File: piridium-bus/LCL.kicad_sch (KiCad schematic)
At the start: 12 parts

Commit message: add R5460 and small bom edits
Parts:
- R?: value 500K -> 510K
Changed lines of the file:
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@@
   (symbol (lib_id "power:GND") (at 148.59 106.68 0) (unit 1)
     (in_bom yes) (on_board yes)
-    (property "Reference" "#PWR?" (id 0) (at 148.59 113.03 0)
+    (property "Reference" "#PWR0105" (id 0) (at 148.59 113.03 0)
       (effects (font (size 1.27 1.27)) hide)
     )
@@
   (symbol (lib_id "power:+3.3VA") (at 125.73 78.74 0) (unit 1)
     (in_bom yes) (on_board yes) (fields_autoplaced)
-    (property "Reference" "#PWR?" (id 0) (at 125.73 82.55 0)
+    (property "Reference" "#PWR0104" (id 0) (at 125.73 82.55 0)
       (effects (font (size 1.27 1.27)) hide)
     )
@@
   (symbol (lib_id "power:GND") (at 95.25 87.63 0) (unit 1)
     (in_bom yes) (on_board yes)
-    (property "Reference" "#PWR?" (id 0) (at 95.25 93.98 0)
+    (property "Reference" "#PWR0108" (id 0) (at 95.25 93.98 0)
       (effects (font (size 1.27 1.27)) hide)
     )
@@
   (symbol (lib_id "power:+3.3VA") (at 95.25 80.01 0) (unit 1)
     (in_bom yes) (on_board yes)
-    (property "Reference" "#PWR?" (id 0) (at 95.25 83.82 0)
+    (property "Reference" "#PWR0107" (id 0) (at 95.25 83.82 0)
       (effects (font (size 1.27 1.27)) hide)
     )
@@
     (in_bom yes) (on_board yes)
     (property "Reference" "R?" (id 0) (at 120.65 96.52 90))
-    (property "Value" "500K" (id 1) (at 120.65 99.06 90))
+    (property "Value" "510K" (id 1) (at 120.65 99.06 90))
     (property "Footprint" "Resistor_SMD:R_0805_2012Metric" (id 2) (at 120.65 100.838 90)
       (effects (font (size 1.27 1.27)) hide)
@@
   (symbol (lib_id "power:+3.3VA") (at 106.68 93.98 0) (unit 1)
     (in_bom yes) (on_board yes)
-    (property "Reference" "#PWR?" (id 0) (at 106.68 97.79 0)
-      (effects (font (size 1.27 1.27)) hide)
-    )
+    (property "Reference" "#PWR0106" (id 0) (at 106.68 97.79 0)
+      (effects (font (size 1.27 1.27)) hide)
+    )

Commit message: battery sch finish
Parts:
- gave numbers to parts that had none: 12
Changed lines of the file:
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@@
   (symbol (lib_id "Transistor_FET:IRF7404") (at 115.57 73.66 270) (mirror x) (unit 1)
     (in_bom yes) (on_board yes)
-    (property "Reference" "Q?" (id 0) (at 115.57 64.9732 90))
+    (property "Reference" "Q9" (id 0) (at 115.57 64.9732 90))
     (property "Value" "DMP3015LSSQ" (id 1) (at 115.57 67.2846 90))
     (property "Footprint" "Package_SO:SOIC-8_3.9x4.9mm_P1.27mm" (id 2) (at 113.665 68.58 0)
@@
   (symbol (lib_id "power:GND") (at 148.59 106.68 0) (unit 1)
     (in_bom yes) (on_board yes)
-    (property "Reference" "#PWR0105" (id 0) (at 148.59 113.03 0)
+    (property "Reference" "#PWR068" (id 0) (at 148.59 113.03 0)
       (effects (font (size 1.27 1.27)) hide)
     )
@@
   (symbol (lib_id "power:+3.3VA") (at 125.73 78.74 0) (unit 1)
     (in_bom yes) (on_board yes) (fields_autoplaced)
-    (property "Reference" "#PWR0104" (id 0) (at 125.73 82.55 0)
+    (property "Reference" "#PWR067" (id 0) (at 125.73 82.55 0)
       (effects (font (size 1.27 1.27)) hide)
     )
@@
   (symbol (lib_id "Device:R") (at 110.49 74.93 0) (mirror y) (unit 1)
     (in_bom yes) (on_board yes)
-    (property "Reference" "R?" (id 0) (at 109.22 74.93 0)
+    (property "Reference" "R43" (id 0) (at 109.22 74.93 0)
       (effects (font (size 1.27 1.27)) (justify left))
     )
@@
   (symbol (lib_id "74xGxx:SN74LVC1G14DBV") (at 106.68 99.06 0) (unit 1)
     (in_bom yes) (on_board yes)
-    (property "Reference" "U?" (id 0) (at 102.87 102.87 0)
+    (property "Reference" "U13" (id 0) (at 102.87 102.87 0)
       (effects (font (size 1.27 1.27)) (justify right))
     )
@@
   (symbol (lib_id "Transistor_FET:2N7002") (at 118.11 83.82 0) (mirror y) (unit 1)
     (in_bom yes) (on_board yes)
-    (property "Reference" "Q?" (id 0) (at 112.903 82.6516 0)
+    (property "Reference" "Q10" (id 0) (at 112.903 82.6516 0)
       (effects (font (size 1.27 1.27)) (justify left))
     )
@@
   (symbol (lib_id "Device:R") (at 148.59 71.12 270) (unit 1)
     (in_bom yes) (on_board yes)
-    (property "Reference" "R?" (id 0) (at 148.59 68.58 90))
+    (property "Reference" "R47" (id 0) (at 148.59 68.58 90))
     (property "Value" "10m" (id 1) (at 148.59 71.12 90))
     (property "Footprint" "Resistor_SMD:R_1206_3216Metric" (id 2) (at 148.59 69.342 90)
@@
   (symbol (lib_id "Device:C") (at 95.25 83.82 0) (unit 1)
     (in_bom yes) (on_board yes)
-    (property "Reference" "C?" (id 0) (at 98.171 82.6516 0)
+    (property "Reference" "C32" (id 0) (at 98.171 82.6516 0)
       (effects (font (size 1.27 1.27)) (justify left))
     )
@@
   (symbol (lib_id "Device:R") (at 132.08 88.9 0) (unit 1)
     (in_bom yes) (on_board yes)
-    (property "Reference" "R?" (id 0) (at 133.35 88.9 0)
+    (property "Reference" "R46" (id 0) (at 133.35 88.9 0)
       (effects (font (size 1.27 1.27)) (justify left))
     )
@@
   (symbol (lib_id "Device:C") (at 124.46 102.87 0) (mirror y) (unit 1)
     (in_bom yes) (on_board yes)
-    (property "Reference" "C?" (id 0) (at 121.92 101.6 0)
+    (property "Reference" "C33" (id 0) (at 121.92 101.6 0)
       (effects (font (size 1.27 1.27)) (justify left))
     )
@@
   (symbol (lib_id "power:GND") (at 95.25 87.63 0) (unit 1)
     (in_bom yes) (on_board yes)
-    (property "Reference" "#PWR0108" (id 0) (at 95.25 93.98 0)
+    (property "Reference" "#PWR065" (id 0) (at 95.25 93.98 0)
       (effects (font (size 1.27 1.27)) hide)
     )
@@
   (symbol (lib_id "Transistor_FET:2N7002") (at 129.54 99.06 0) (unit 1)
     (in_bom yes) (on_board yes)
-    (property "Reference" "Q?" (id 0) (at 134.747 97.8916 0)
+    (property "Reference" "Q11" (id 0) (at 134.747 97.8916 0)
       (effects (font (size 1.27 1.27)) (justify left))
     )
@@
   (symbol (lib_id "Device:R") (at 125.73 82.55 0) (unit 1)
     (in_bom yes) (on_board yes)
-    (property "Reference" "R?" (id 0) (at 127 82.55 0)
+    (property "Reference" "R45" (id 0) (at 127 82.55 0)
       (effects (font (size 1.27 1.27)) (justify left))
     )
@@
   (symbol (lib_id "power:+3.3VA") (at 95.25 80.01 0) (unit 1)
     (in_bom yes) (on_board yes)
-    (property "Reference" "#PWR0107" (id 0) (at 95.25 83.82 0)
+    (property "Reference" "#PWR064" (id 0) (at 95.25 83.82 0)
       (effects (font (size 1.27 1.27)) hide)
     )
@@
   (symbol (lib_id "Device:R") (at 120.65 99.06 90) (unit 1)
     (in_bom yes) (on_board yes)
-    (property "Reference" "R?" (id 0) (at 120.65 96.52 90))
+    (property "Reference" "R44" (id 0) (at 120.65 96.52 90))
     (property "Value" "510K" (id 1) (at 120.65 99.06 90))
     (property "Footprint" "Resistor_SMD:R_0805_2012Metric" (id 2) (at 120.65 100.838 90)
@@
   (symbol (lib_id "piridium-bus:MAX4373F") (at 148.59 76.2 0) (unit 1)
     (in_bom yes) (on_board yes)
-    (property "Reference" "U?" (id 0) (at 153.67 72.39 0)
+    (property "Reference" "U14" (id 0) (at 153.67 72.39 0)
       (effects (font (size 1.27 1.27)) (justify left))
     )
@@
   (symbol (lib_id "power:+3.3VA") (at 106.68 93.98 0) (unit 1)
     (in_bom yes) (on_board yes)
-    (property "Reference" "#PWR0106" (id 0) (at 106.68 97.79 0)
-      (effects (font (size 1.27 1.27)) hide)
-    )
+    (property "Reference" "#PWR066" (id 0) (at 106.68 97.79 0)
+      (effects (font (size 1.27 1.27)) hide)
+    )

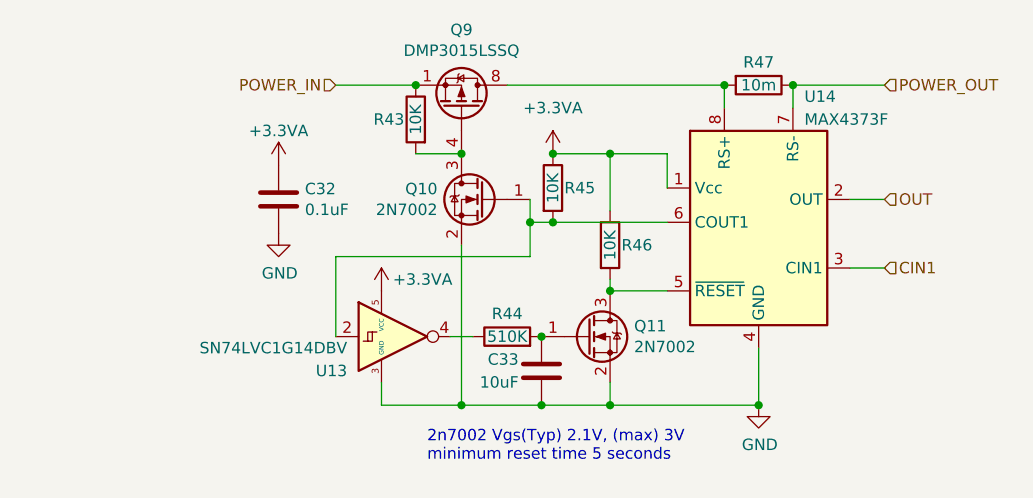
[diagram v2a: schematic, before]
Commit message: correct max4373 implementation, #5 and #4
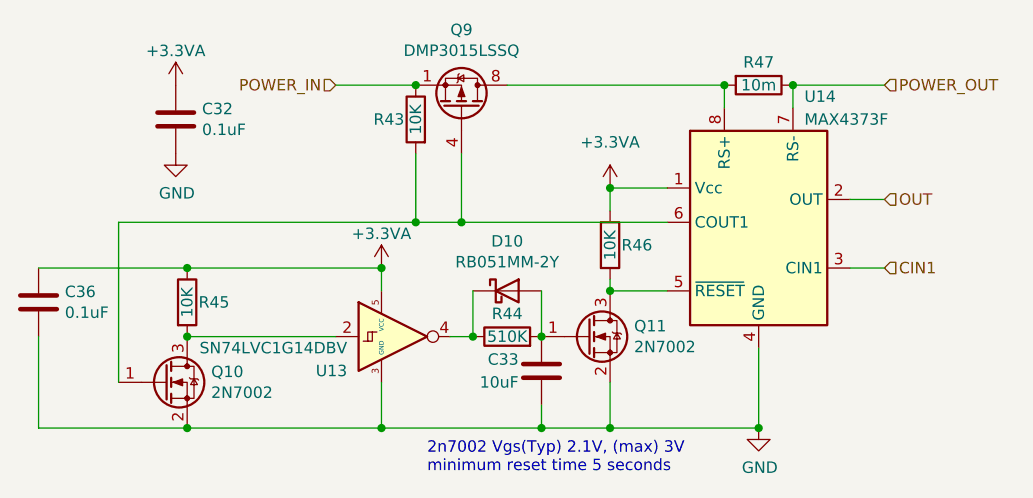
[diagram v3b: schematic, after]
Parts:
- added C36: 0.1uF, Capacitor_SMD:C_0805_2012Metric, symbol Device:C
- added D10: RB051MM-2Y, Diode_SMD:D_SOD-123F, symbol Device:D_Schottky
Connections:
- net +3.3VA: now also C36.1
- net GND: now also C36.2
- net at Q9.4 (G), R43.2: now also Q10.1 (G), U14.6 (COUT1); no longer Q10.3 (D)
- net at R45.2, U13.2: now also Q10.3 (D); no longer Q10.1 (G), U14.6 (COUT1)
- net at R44.1, U13.4: now also D10.1 (K)
- net at C33.1, Q11.1 (G), R44.2: now also D10.2 (A)
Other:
- moved on the sheet: C32

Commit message: mcp3208 constant reference
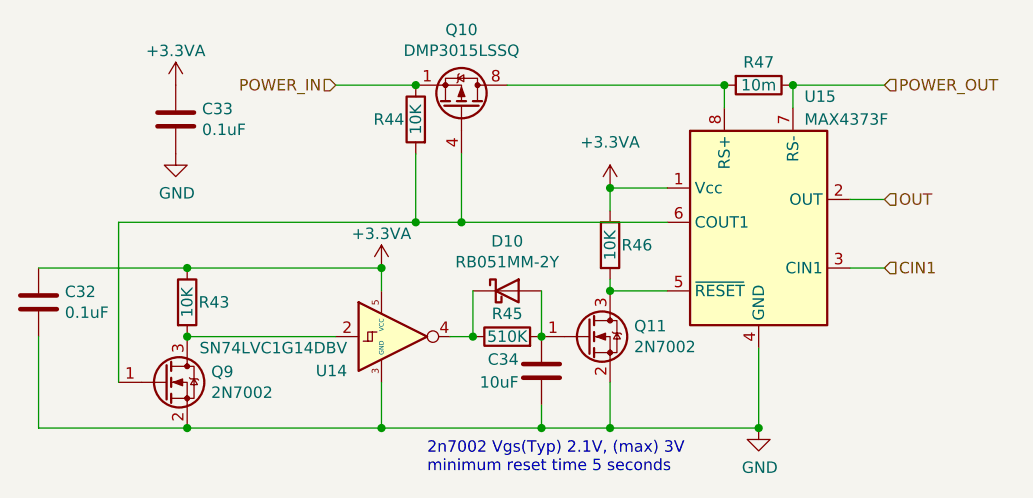
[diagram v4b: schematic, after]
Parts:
- renumbered C36 to C32, C32 to C33, C33 to C34, Q9 to Q10, Q10 to Q9, R45 to R43, R43 to R44, R44 to R45, U13 to U14, U14 to U15
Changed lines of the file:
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@@
   (symbol (lib_id "Transistor_FET:IRF7404") (at 115.57 73.66 270) (mirror x) (unit 1)
     (in_bom yes) (on_board yes)
-    (property "Reference" "Q9" (id 0) (at 115.57 64.9732 90))
+    (property "Reference" "Q10" (id 0) (at 115.57 64.9732 90))
     (property "Value" "DMP3015LSSQ" (id 1) (at 115.57 67.2846 90))
     (property "Footprint" "Package_SO:SOIC-8_3.9x4.9mm_P1.27mm" (id 2) (at 113.665 68.58 0)
@@
   (symbol (lib_id "power:GND") (at 148.59 109.22 0) (unit 1)
     (in_bom yes) (on_board yes)
-    (property "Reference" "#PWR068" (id 0) (at 148.59 115.57 0)
+    (property "Reference" "#PWR070" (id 0) (at 148.59 115.57 0)
       (effects (font (size 1.27 1.27)) hide)
     )
@@
   (symbol (lib_id "power:+3.3VA") (at 132.08 82.55 0) (unit 1)
     (in_bom yes) (on_board yes) (fields_autoplaced)
-    (property "Reference" "#PWR067" (id 0) (at 132.08 86.36 0)
+    (property "Reference" "#PWR069" (id 0) (at 132.08 86.36 0)
       (effects (font (size 1.27 1.27)) hide)
     )
@@
   (symbol (lib_id "Device:R") (at 85.09 95.25 0) (unit 1)
     (in_bom yes) (on_board yes)
-    (property "Reference" "R45" (id 0) (at 86.36 95.25 0)
+    (property "Reference" "R43" (id 0) (at 86.36 95.25 0)
       (effects (font (size 1.27 1.27)) (justify left))
     )
@@
   (symbol (lib_id "Device:R") (at 110.49 74.93 0) (mirror y) (unit 1)
     (in_bom yes) (on_board yes)
-    (property "Reference" "R43" (id 0) (at 109.22 74.93 0)
+    (property "Reference" "R44" (id 0) (at 109.22 74.93 0)
       (effects (font (size 1.27 1.27)) (justify left))
     )
@@
   (symbol (lib_id "74xGxx:SN74LVC1G14DBV") (at 106.68 99.06 0) (unit 1)
     (in_bom yes) (on_board yes)
-    (property "Reference" "U13" (id 0) (at 102.87 102.87 0)
+    (property "Reference" "U14" (id 0) (at 102.87 102.87 0)
       (effects (font (size 1.27 1.27)) (justify right))
     )
@@
   (symbol (lib_id "Device:C") (at 83.82 74.93 0) (unit 1)
     (in_bom yes) (on_board yes)
-    (property "Reference" "C32" (id 0) (at 86.741 73.7616 0)
+    (property "Reference" "C33" (id 0) (at 86.741 73.7616 0)
       (effects (font (size 1.27 1.27)) (justify left))
     )
@@
   (symbol (lib_id "Transistor_FET:2N7002") (at 82.55 104.14 0) (unit 1)
     (in_bom yes) (on_board yes)
-    (property "Reference" "Q10" (id 0) (at 87.757 102.9716 0)
+    (property "Reference" "Q9" (id 0) (at 87.757 102.9716 0)
       (effects (font (size 1.27 1.27)) (justify left))
     )
@@
   (symbol (lib_id "Device:C") (at 124.46 102.87 0) (mirror y) (unit 1)
     (in_bom yes) (on_board yes)
-    (property "Reference" "C33" (id 0) (at 121.92 101.6 0)
+    (property "Reference" "C34" (id 0) (at 121.92 101.6 0)
       (effects (font (size 1.27 1.27)) (justify left))
     )
@@
   (symbol (lib_id "power:GND") (at 83.82 78.74 0) (unit 1)
     (in_bom yes) (on_board yes)
-    (property "Reference" "#PWR065" (id 0) (at 83.82 85.09 0)
+    (property "Reference" "#PWR067" (id 0) (at 83.82 85.09 0)
       (effects (font (size 1.27 1.27)) hide)
     )
@@
   (symbol (lib_id "power:+3.3VA") (at 83.82 71.12 0) (unit 1)
     (in_bom yes) (on_board yes)
-    (property "Reference" "#PWR064" (id 0) (at 83.82 74.93 0)
+    (property "Reference" "#PWR066" (id 0) (at 83.82 74.93 0)
       (effects (font (size 1.27 1.27)) hide)
     )
@@
   (symbol (lib_id "Device:R") (at 120.65 99.06 90) (unit 1)
     (in_bom yes) (on_board yes)
-    (property "Reference" "R44" (id 0) (at 120.65 96.52 90))
+    (property "Reference" "R45" (id 0) (at 120.65 96.52 90))
     (property "Value" "510K" (id 1) (at 120.65 99.06 90))
     (property "Footprint" "Resistor_SMD:R_0805_2012Metric" (id 2) (at 120.65 100.838 90)
@@
   (symbol (lib_id "Device:C") (at 68.58 95.25 0) (unit 1)
     (in_bom yes) (on_board yes)
-    (property "Reference" "C36" (id 0) (at 71.501 94.0816 0)
+    (property "Reference" "C32" (id 0) (at 71.501 94.0816 0)
       (effects (font (size 1.27 1.27)) (justify left))
     )
@@
   (symbol (lib_id "piridium-bus:MAX4373F") (at 148.59 76.2 0) (unit 1)
     (in_bom yes) (on_board yes)
-    (property "Reference" "U14" (id 0) (at 153.67 72.39 0)
+    (property "Reference" "U15" (id 0) (at 153.67 72.39 0)
       (effects (font (size 1.27 1.27)) (justify left))
     )
@@
   (symbol (lib_id "power:+3.3VA") (at 106.68 91.44 0) (unit 1)
     (in_bom yes) (on_board yes)
-    (property "Reference" "#PWR066" (id 0) (at 106.68 95.25 0)
-      (effects (font (size 1.27 1.27)) hide)
-    )
+    (property "Reference" "#PWR068" (id 0) (at 106.68 95.25 0)
+      (effects (font (size 1.27 1.27)) hide)
+    )

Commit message: pull down on/off instead of up
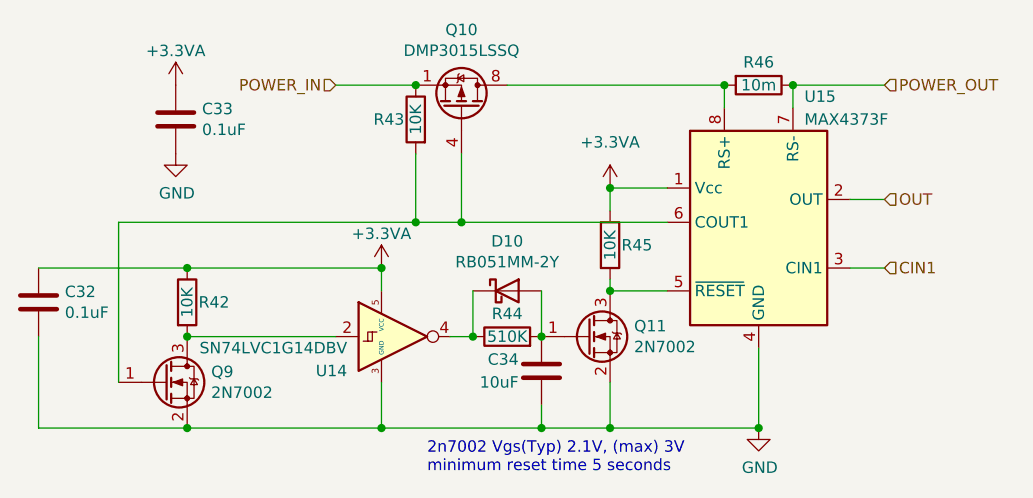
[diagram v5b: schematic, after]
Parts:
- renumbered R43 to R42, R44 to R43, R45 to R44, R46 to R45, R47 to R46
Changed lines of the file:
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@@
   (symbol (lib_id "power:GND") (at 148.59 109.22 0) (unit 1)
     (in_bom yes) (on_board yes)
-    (property "Reference" "#PWR070" (id 0) (at 148.59 115.57 0)
+    (property "Reference" "#PWR069" (id 0) (at 148.59 115.57 0)
       (effects (font (size 1.27 1.27)) hide)
     )
@@
   (symbol (lib_id "power:+3.3VA") (at 132.08 82.55 0) (unit 1)
     (in_bom yes) (on_board yes) (fields_autoplaced)
-    (property "Reference" "#PWR069" (id 0) (at 132.08 86.36 0)
+    (property "Reference" "#PWR068" (id 0) (at 132.08 86.36 0)
       (effects (font (size 1.27 1.27)) hide)
     )
@@
   (symbol (lib_id "Device:R") (at 85.09 95.25 0) (unit 1)
     (in_bom yes) (on_board yes)
-    (property "Reference" "R43" (id 0) (at 86.36 95.25 0)
+    (property "Reference" "R42" (id 0) (at 86.36 95.25 0)
       (effects (font (size 1.27 1.27)) (justify left))
     )
@@
   (symbol (lib_id "Device:R") (at 110.49 74.93 0) (mirror y) (unit 1)
     (in_bom yes) (on_board yes)
-    (property "Reference" "R44" (id 0) (at 109.22 74.93 0)
+    (property "Reference" "R43" (id 0) (at 109.22 74.93 0)
       (effects (font (size 1.27 1.27)) (justify left))
     )
@@
   (symbol (lib_id "Device:R") (at 148.59 71.12 270) (unit 1)
     (in_bom yes) (on_board yes)
-    (property "Reference" "R47" (id 0) (at 148.59 68.58 90))
+    (property "Reference" "R46" (id 0) (at 148.59 68.58 90))
     (property "Value" "10m" (id 1) (at 148.59 71.12 90))
     (property "Footprint" "Resistor_SMD:R_1206_3216Metric" (id 2) (at 148.59 69.342 90)
@@
   (symbol (lib_id "Device:R") (at 132.08 88.9 0) (unit 1)
     (in_bom yes) (on_board yes)
-    (property "Reference" "R46" (id 0) (at 133.35 88.9 0)
+    (property "Reference" "R45" (id 0) (at 133.35 88.9 0)
       (effects (font (size 1.27 1.27)) (justify left))
     )
@@
   (symbol (lib_id "power:GND") (at 83.82 78.74 0) (unit 1)
     (in_bom yes) (on_board yes)
-    (property "Reference" "#PWR067" (id 0) (at 83.82 85.09 0)
+    (property "Reference" "#PWR066" (id 0) (at 83.82 85.09 0)
       (effects (font (size 1.27 1.27)) hide)
     )
@@
   (symbol (lib_id "power:+3.3VA") (at 83.82 71.12 0) (unit 1)
     (in_bom yes) (on_board yes)
-    (property "Reference" "#PWR066" (id 0) (at 83.82 74.93 0)
+    (property "Reference" "#PWR065" (id 0) (at 83.82 74.93 0)
       (effects (font (size 1.27 1.27)) hide)
     )
@@
   (symbol (lib_id "Device:R") (at 120.65 99.06 90) (unit 1)
     (in_bom yes) (on_board yes)
-    (property "Reference" "R45" (id 0) (at 120.65 96.52 90))
+    (property "Reference" "R44" (id 0) (at 120.65 96.52 90))
     (property "Value" "510K" (id 1) (at 120.65 99.06 90))
     (property "Footprint" "Resistor_SMD:R_0805_2012Metric" (id 2) (at 120.65 100.838 90)
@@
   (symbol (lib_id "power:+3.3VA") (at 106.68 91.44 0) (unit 1)
     (in_bom yes) (on_board yes)
-    (property "Reference" "#PWR068" (id 0) (at 106.68 95.25 0)
-      (effects (font (size 1.27 1.27)) hide)
-    )
+    (property "Reference" "#PWR067" (id 0) (at 106.68 95.25 0)
+      (effects (font (size 1.27 1.27)) hide)
+    )
